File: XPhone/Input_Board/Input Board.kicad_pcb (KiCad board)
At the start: 2 copper layers, 100 x 100 mm, 94 parts, among them J1 AUDIO, J10 ENV, J11 PULSE, J12 PULSE, J13 Power In, J14 Power Out, J2 AUDIO, J3 ENV, J4 ENV, J5 PULSE, J6 PULSE, J7 AUDIO, J8 AUDIO, J9 ENV, Q1 BC847CW, Q2 BC847CW, Q3 BC847CW, Q4 BC847CW, Q5 BC847CW, Q6 BC847CW, Q7 BC847CW, Q8 BC847CW, U1 LM833, U2 78L05, U3 TL084, U4 74HC14, U5 LM833

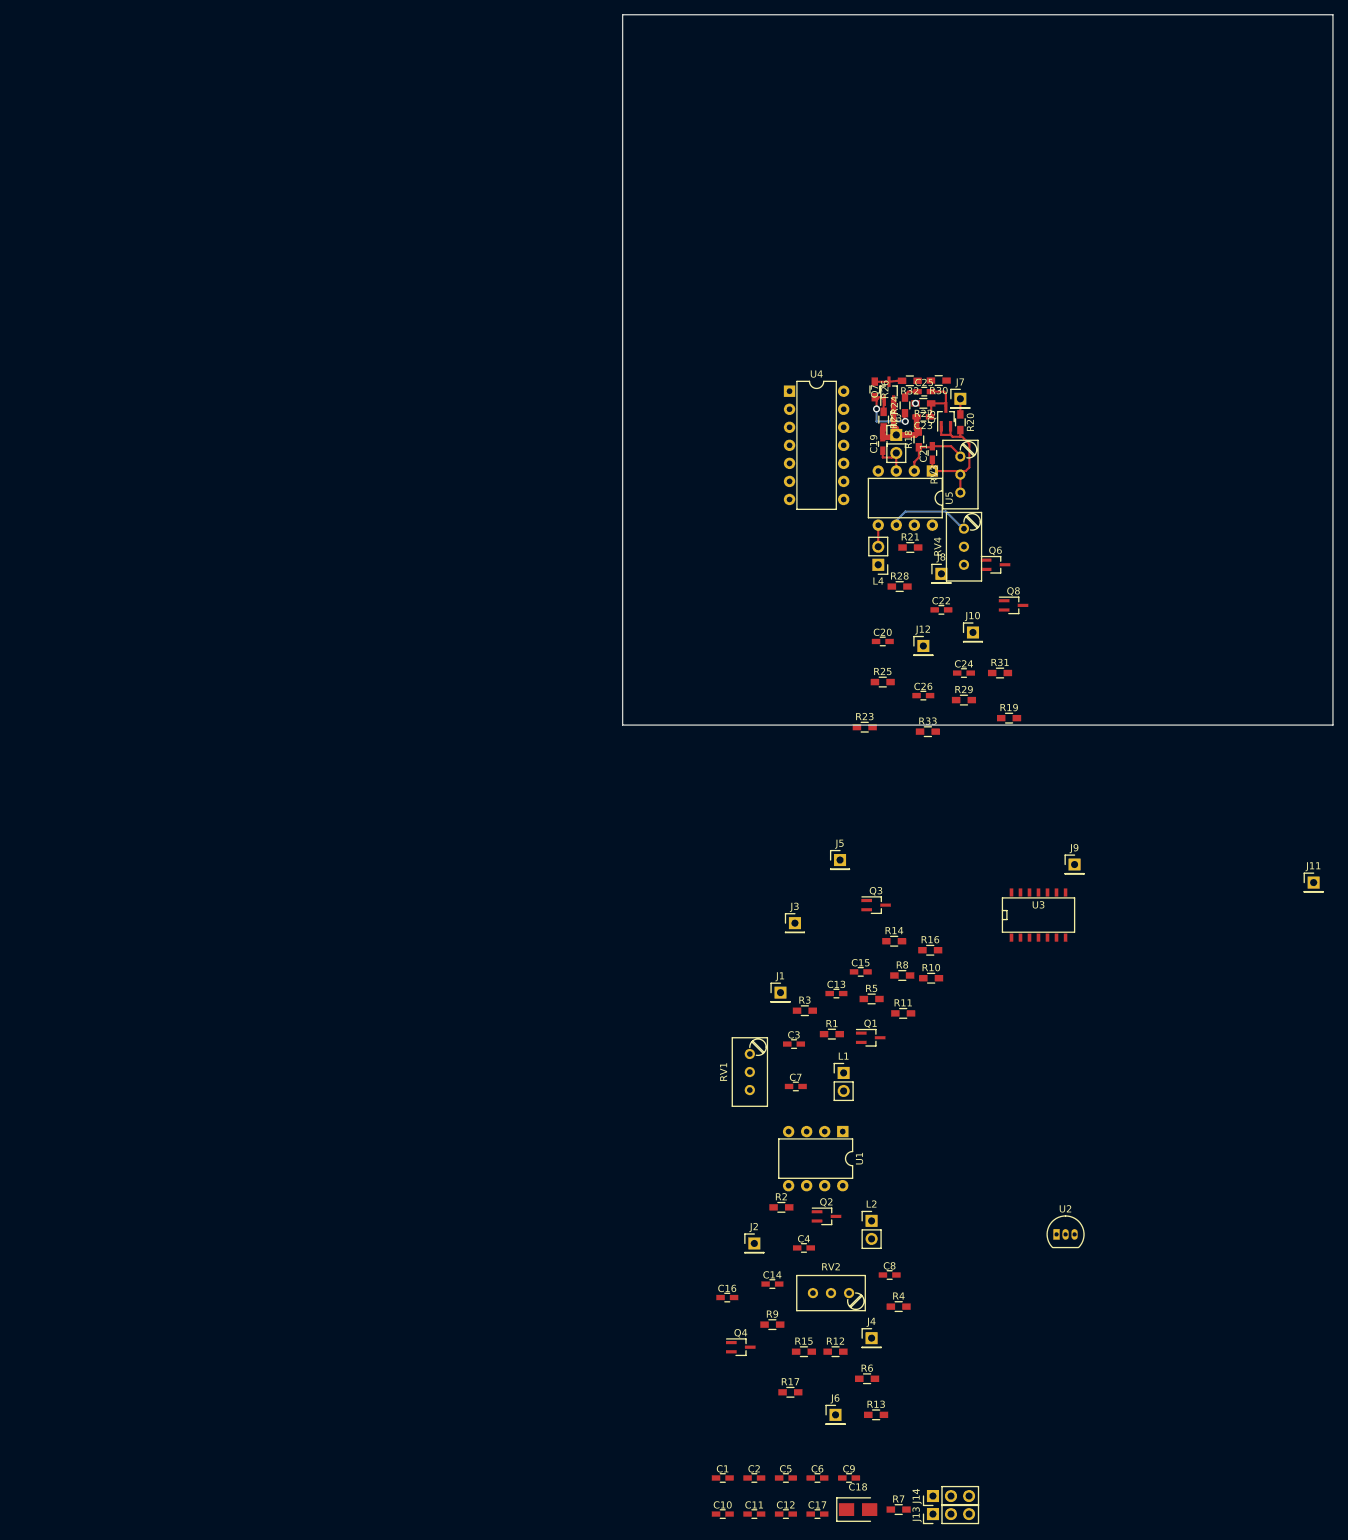
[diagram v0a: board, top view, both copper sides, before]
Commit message: XPhone/Input_Board L4 circuit
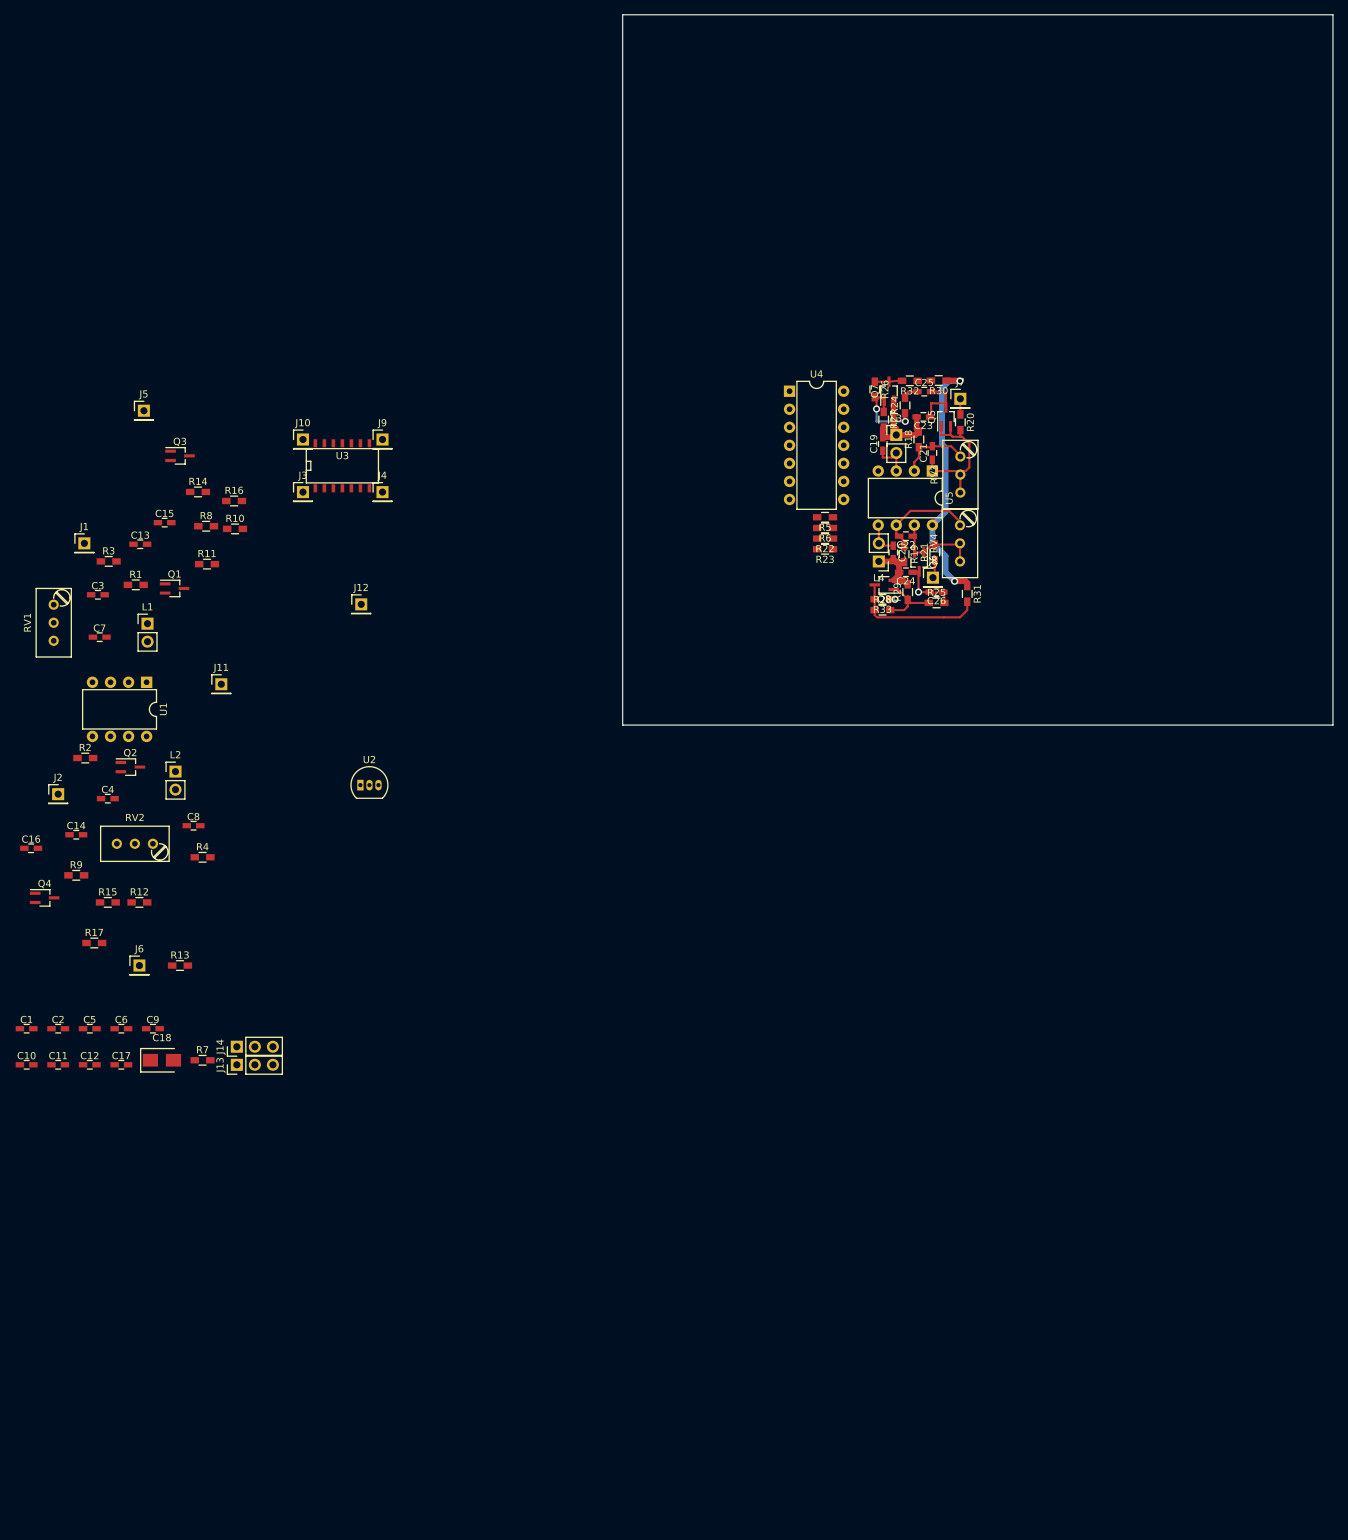
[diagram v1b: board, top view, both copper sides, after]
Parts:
- moved J11 156.3 mm to (-56.5, 94.2)
- moved J4 137.6 mm to (-33.8, 67.2)
- moved R6 119.9 mm to (28.5, 72.2), turned to 180 degrees
- moved C15 116.6 mm to (-64.5, 71.5)
- moved C3 116.6 mm to (-73.9, 81.7)
- moved C4 116.6 mm to (-72.5, 110.4)
- moved C8 116.6 mm to (-60.4, 114.2)
- moved Q4 116.6 mm to (-81.4, 124.3)
- moved R16 116.6 mm to (-54.7, 68.4)
- moved U2 116.6 mm to (-36.9, 108.5)
- moved C1 116.6 mm to (-83.9, 142.7)
- moved C10 116.6 mm to (-83.9, 147.8)
- moved C11 116.6 mm to (-79.5, 147.8)
- moved C12 116.6 mm to (-75.0, 147.8)
- moved C13 116.6 mm to (-67.9, 74.5)
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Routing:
- net +12V: track 0.00 -> 36.6 mm, vias 0 -> 2
- net Net-(Q8-Pad3): track 0.00 -> 19.0 mm
- net Net-(C22-Pad1): track 0.00 -> 13.5 mm
- net GNDA: track 14.8 -> 24.5 mm
- net Net-(Q8-Pad1): track 0.00 -> 9.45 mm
- net Net-(C24-Pad1): track 0.00 -> 5.75 mm, vias 0 -> 1
- net Net-(C22-Pad2): track 11.5 -> 14.4 mm
- net Net-(J8-Pad1): track 0.00 -> 2.56 mm
- net Net-(C20-Pad1): track 2.54 -> 4.77 mm
- net Net-(C26-Pad1): track 0.00 -> 1.59 mm
- net Net-(R33-Pad1): track 0.00 -> 0.68 mm, vias 0 -> 1
- net V_ENV_BIAS: track 0.17 -> 0.00 mm, vias 1 -> 0

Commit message: XPhone/Input_Board getting close to being done with layout.
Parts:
- L1: moved to B.Cu
- moved Q4 113.4 mm to (13.2, 61.7)
- moved R17 110.8 mm to (14.0, 63.8), turned to 180 degrees
- moved R15 109.4 mm to (15.0, 59.2), turned to 270 degrees
- moved C16 105.9 mm to (6.86, 61.7), turned to 270 degrees
- moved R9 105.2 mm to (8.64, 59.9), turned to 90 degrees
- moved J6 104.1 mm to (29.8, 98.4)
- moved J5 103.9 mm to (27.3, 98.4)
- moved R12 103.4 mm to (11.7, 59.2), turned to 180 degrees
- moved R13 101.4 mm to (9.65, 62.5)
- moved C14 100.6 mm to (9.65, 64.3)
- moved C4 95.0 mm to (12.2, 67.3), turned to 90 degrees
- moved R2 94.1 mm to (10.7, 67.1), turned to 90 degrees
- moved J11 89.0 mm to (32.4, 98.4)
- moved C3 87.8 mm to (14.0, 82.5), turned to 270 degrees
- moved L2 87.2 mm to (14.2, 66.0)
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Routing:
- net GNDA: track 24.5 -> 52.1 mm, vias 0 -> 1
- net Net-(C7-Pad1): track 0.00 -> 20.1 mm
- net Net-(C8-Pad2): track 0.00 -> 14.0 mm
- net Net-(C8-Pad1): track 0.00 -> 13.2 mm
- net Net-(C7-Pad2): track 0.00 -> 10.5 mm
- net Net-(Q4-Pad1): track 0.00 -> 7.99 mm
- net Net-(Q4-Pad3): track 0.00 -> 7.12 mm
- net Net-(C13-Pad1): track 0.00 -> 6.09 mm, vias 0 -> 1
- net Net-(Q3-Pad3): track 0.00 -> 5.40 mm
- net Net-(C14-Pad1): track 0.00 -> 5.36 mm, vias 0 -> 1
- net Net-(Q3-Pad1): track 0.00 -> 5.07 mm
- net Net-(C3-Pad1): track 0.00 -> 4.96 mm
- net Net-(C16-Pad1): track 0.00 -> 3.21 mm
- net Net-(C24-Pad1): track 5.75 -> 3.18 mm, vias 1 -> 0
- net Net-(J2-Pad1): track 0.00 -> 2.26 mm, vias 0 -> 1
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
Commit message: XPhone/Input_Board ^layout; using wide TO-92; close to done
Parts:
- U2: footprint TO_SOT_Packages_THT:TO-92_Inline_Narrow_Oval -> TO_SOT_Packages_THT:TO-92_Inline_Wide
- moved C11 143.3 mm to (30.6, 31.9)
- moved C17 134.7 mm to (38.4, 41.8), turned to 90 degrees
- moved C12 133.5 mm to (27.7, 38.6), turned to 180 degrees
- moved R7 128.9 mm to (31.7, 35.8), turned to 90 degrees
- moved C10 126.4 mm to (11.7, 42.4), turned to 90 degrees
- moved C1 123.7 mm to (14.6, 42.7), turned to 90 degrees
- moved C2 123.0 mm to (17.8, 42.5), turned to 90 degrees
- moved C5 121.7 mm to (20.3, 42.8), turned to 90 degrees
- moved C6 121.3 mm to (24.0, 42.8), turned to 90 degrees
- moved C9 120.7 mm to (27.3, 42.8), turned to 90 degrees
- moved C18 113.2 mm to (30.5, 57.9), turned to 90 degrees
- moved J13 108.7 mm to (22.2, 51.6)
- moved J14 104.2 mm to (22.2, 54.1)
- moved U2 62.3 mm to (26.3, 58.7), turned to 180 degrees
- moved R6 46.1 mm to (18.7, 84.3)
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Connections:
- U3 pad 1: Net-(J3-Pad1) -> Net-(J4-Pad1)
- U3 pad 10: Net-(C23-Pad1) -> Net-(C24-Pad1)
- U3 pad 12: Net-(C24-Pad1) -> Net-(C23-Pad1)
- U3 pad 13: Net-(J10-Pad1) -> Net-(J9-Pad1)
- U3 pad 14: Net-(J10-Pad1) -> Net-(J9-Pad1)
- U3 pad 2: Net-(J3-Pad1) -> Net-(J4-Pad1)
- U3 pad 3: Net-(C13-Pad1) -> Net-(C14-Pad1)
- U3 pad 5: Net-(C14-Pad1) -> Net-(C13-Pad1)
- U3 pad 6: Net-(J4-Pad1) -> Net-(J3-Pad1)
- U3 pad 7: Net-(J4-Pad1) -> Net-(J3-Pad1)
- U3 pad 8: Net-(J9-Pad1) -> Net-(J10-Pad1)
- U3 pad 9: Net-(J9-Pad1) -> Net-(J10-Pad1)
- U4 pad 1: Net-(R16-Pad1) -> Net-(R17-Pad1)
- U4 pad 11: (no net) -> GND
- U4 pad 12: (no net) -> Net-(J11-Pad1)
- U4 pad 13: (no net) -> Net-(R32-Pad1)
- U4 pad 2: Net-(J5-Pad1) -> Net-(J6-Pad1)
- U4 pad 3: Net-(R17-Pad1) -> GND
- U4 pad 4: Net-(J6-Pad1) -> (no net)
- U4 pad 5: Net-(R32-Pad1) -> Net-(R16-Pad1)
- U4 pad 6: Net-(J11-Pad1) -> Net-(J5-Pad1)
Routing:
- net V_ENV_BIAS: track 0.00 -> 20.0 mm, vias 0 -> 2
- net GND: track 0.00 -> 11.2 mm
- net Net-(R17-Pad1): track 0.00 -> 6.56 mm
- net -12V: track 0.00 -> 2.54 mm
- net +12V: track 36.5 -> 39.0 mm
- net Net-(C14-Pad1): track 5.36 -> 7.36 mm
- net Net-(C24-Pad1): track 3.18 -> 5.13 mm
- net Net-(C13-Pad1): track 6.09 -> 8.04 mm
- net Net-(C23-Pad1): track 10.2 -> 12.2 mm

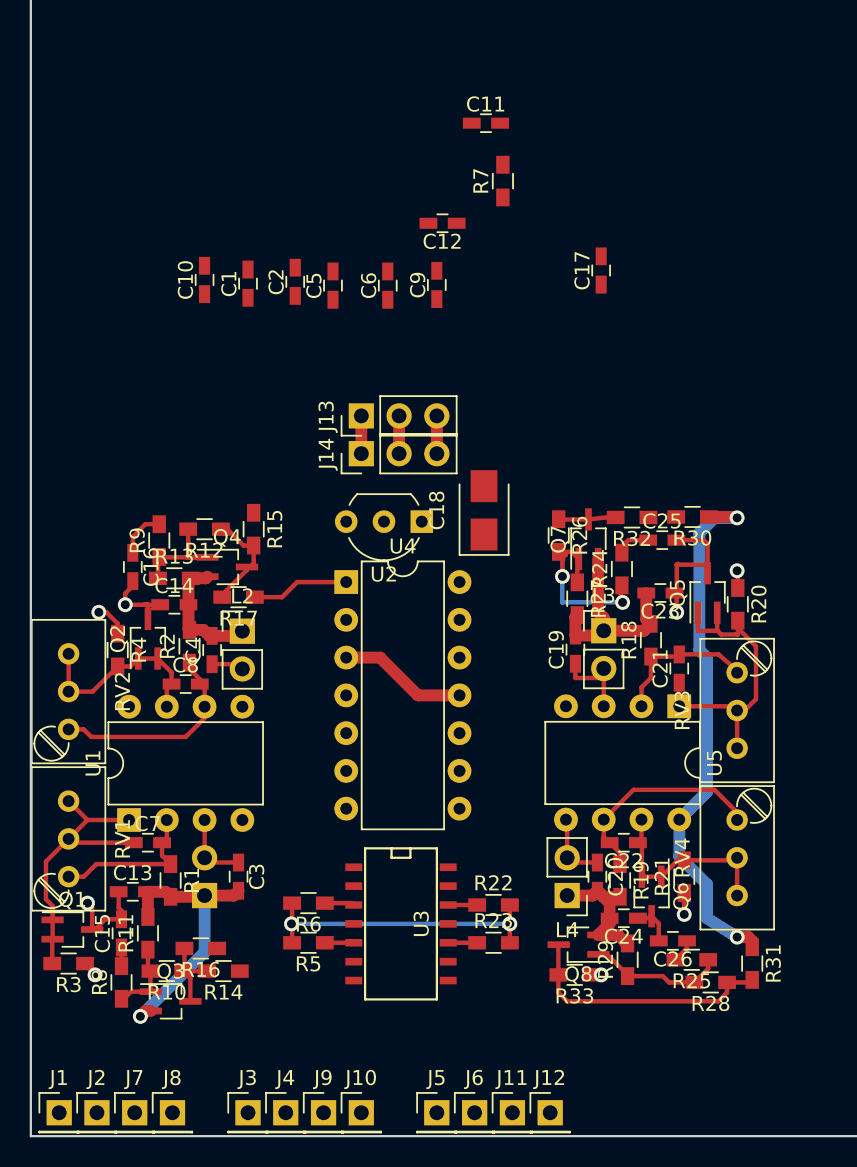
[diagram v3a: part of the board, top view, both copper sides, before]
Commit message: XPhone/Input_Board - just realized I forgot to add V_ENV_BIAS to the circuit; continuing layout...
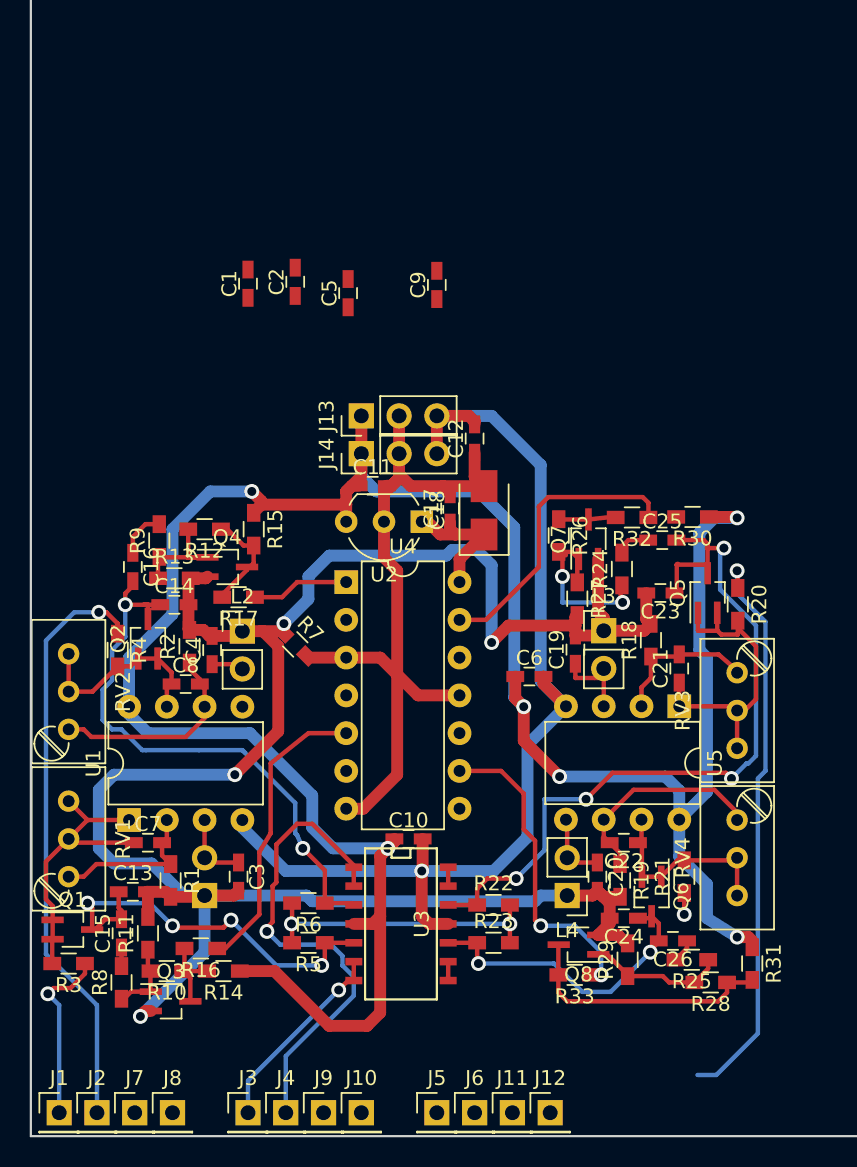
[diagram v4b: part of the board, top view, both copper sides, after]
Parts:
- moved C10 40.0 mm to (25.4, 80.0), turned to 0 degrees
- moved R7 34.1 mm to (17.8, 66.9), turned to 315 degrees
- moved C6 28.0 mm to (33.5, 69.1), turned to 0 degrees
- moved C11 25.5 mm to (23.0, 56.3)
- moved C17 19.0 mm to (28.2, 57.8)
- moved C12 14.6 mm to (29.8, 53.1), turned to 90 degrees
- moved C5 1.14 mm to (21.3, 43.3)
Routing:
- net +12V: track 39.0 -> 164.4 mm, vias 2 -> 6
- net GNDA: track 52.1 -> 142.2 mm, vias 1 -> 4
- net -12V: track 2.54 -> 72.3 mm, vias 0 -> 1
- net Net-(C23-Pad1): track 12.2 -> 53.1 mm, vias 1 -> 4
- net GND: track 11.2 -> 51.2 mm
- net Net-(J2-Pad1): track 2.26 -> 39.8 mm
- net Net-(J7-Pad1): track 1.18 -> 38.5 mm
- net Net-(J4-Pad1): track 0.00 -> 33.3 mm, vias 0 -> 1
- net Net-(C14-Pad1): track 7.36 -> 38.5 mm, vias 1 -> 2
- net Net-(R33-Pad1): track 0.68 -> 21.3 mm, vias 1 -> 2
- net Net-(R16-Pad1): track 0.00 -> 19.9 mm
- net Net-(R32-Pad1): track 0.00 -> 19.6 mm
- net Net-(C13-Pad1): track 8.04 -> 27.6 mm, vias 1 -> 4
- net Net-(C24-Pad1): track 5.13 -> 21.0 mm, vias 0 -> 2
- net Net-(J3-Pad1): track 0.00 -> 13.3 mm, vias 0 -> 1
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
